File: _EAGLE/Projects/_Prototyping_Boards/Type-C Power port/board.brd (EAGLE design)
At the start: 12.5 x 19 mm, 2 parts, among them J1 TYPE-C-31-M-17

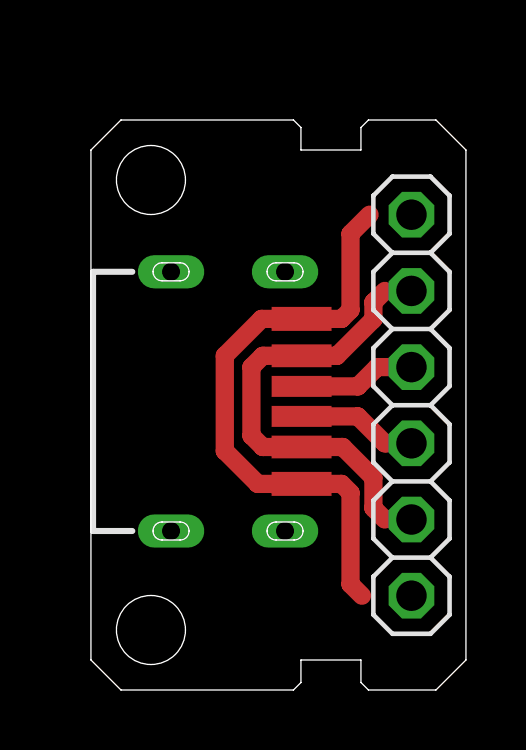
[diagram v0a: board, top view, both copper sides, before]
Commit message: Type-C power port design error fix
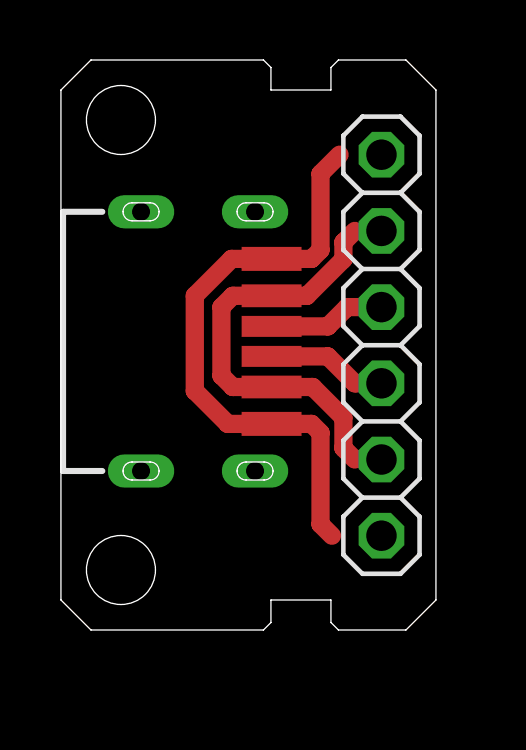
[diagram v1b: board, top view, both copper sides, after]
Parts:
- moved JP1 2.24 mm to (10.7, 9.49)
- moved J1 2.24 mm to (6.62, 9.62)
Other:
- board text added: "1.0"
- board text added: "2.0"
- board text added: "3.5"
- board text added: "7.0"
